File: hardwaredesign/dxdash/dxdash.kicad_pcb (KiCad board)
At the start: 2 copper layers, 112 parts, among them J11 spare, J12 spare, J13 spare, J14 spare, J15 spare, J16 uC_NRST, J17 3V3_uC, J18 SWO, J2 Conn_01x08_Pin, J3 CAN, J4 DEBUG, J5 UART, J6 12V_in, J8 Power Low Side Outputs, J9 Temps, Q2 NCV8402xST, Q3 NCV8402xST, U2 SN65HVD234, U3 STM32F103RETx, U4 TPS54302, U6 AMS1117-3.3, U7 74HCT04, Y2 8MHz

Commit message: controller board added features
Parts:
- removed C77, C78, C79: 100nF, Capacitor_SMD:C_1206_3216Metric_Pad1.33x1.80mm_HandSolder
- removed J11, J13, J14, J15: spare, Connector_PinHeader_2.54mm:PinHeader_1x06_P2.54mm_Vertical
- removed J3: CAN, Connector_PinHeader_2.54mm:PinHeader_1x03_P2.54mm_Vertical
- removed J9: Temps, Connector_PinHeader_2.54mm:PinHeader_1x04_P2.54mm_Vertical
- removed JP1: SolderJumper3V3together, Jumper:SolderJumper-2_P1.3mm_Open_TrianglePad1.0x1.5mm
- removed R31, R33, R35: 10k, Resistor_SMD:R_1206_3216Metric_Pad1.30x1.75mm_HandSolder
- removed R32, R34, R36: 47k, Resistor_SMD:R_1206_3216Metric_Pad1.30x1.75mm_HandSolder
- removed TP14, TP23, TP24, TP34, TP36: ~, TestPoint:TestPoint_THTPad_D1.0mm_Drill0.5mm
- added C1: 100n, Capacitor_SMD:C_1206_3216Metric_Pad1.33x1.80mm_HandSolder, F.Cu at (58.1, 77.4)
- added C2: 100nF, Capacitor_SMD:C_1206_3216Metric_Pad1.33x1.80mm_HandSolder, F.Cu at (44.7, 129.5)
- added C3: 100nF, Capacitor_SMD:C_1206_3216Metric_Pad1.33x1.80mm_HandSolder, F.Cu at (44.7, 132.9)
- added H4: MountingHole, MountingHole:MountingHole_3.5mm, F.Cu at (215.8, 133.8)
- added H5: MountingHole, MountingHole:MountingHole_3.5mm, F.Cu at (124.2, 81.2)
- added H6: MountingHole, MountingHole:MountingHole_3.5mm, F.Cu at (227.3, 81.0)
- added H7: MountingHole, MountingHole:MountingHole_3.5mm, F.Cu at (127.7, 147.0)
- added H8: MountingHole, MountingHole:MountingHole_3.5mm, F.Cu at (227.2, 145.1)
- added J1: Conn_01x08_Pin, Connector_PinHeader_2.54mm:PinHeader_1x08_P2.54mm_Vertical, F.Cu at (216.8, 102.5)
- added Q4: BC556, Package_TO_SOT_THT:TO-92_Inline, F.Cu at (40.1, 99.9)
- added Q6: BC546, Package_TO_SOT_THT:TO-92_Inline, F.Cu at (40.1, 105.7)
- added Q7: BC556, Package_TO_SOT_THT:TO-92_Inline, F.Cu at (50.5, 79.0)
- added Q8: BC546, Package_TO_SOT_THT:TO-92_Inline, F.Cu at (50.5, 84.8)
- added R1: 10k, Resistor_SMD:R_1206_3216Metric_Pad1.30x1.75mm_HandSolder, F.Cu at (40.0, 113.0)
- added R10: 4k7, Resistor_SMD:R_1206_3216Metric_Pad1.30x1.75mm_HandSolder, F.Cu at (45.6, 87.3)
- added R2: 1k, Resistor_SMD:R_1206_3216Metric_Pad1.30x1.75mm_HandSolder, F.Cu at (47.6, 98.3)
- added R25: 47k, Resistor_SMD:R_1206_3216Metric_Pad1.30x1.75mm_HandSolder, F.Cu at (45.9, 116.3)
- added R26: 47k, Resistor_SMD:R_1206_3216Metric_Pad1.30x1.75mm_HandSolder, F.Cu at (45.9, 119.6)
- added R27: 47k, Resistor_SMD:R_1206_3216Metric_Pad1.30x1.75mm_HandSolder, F.Cu at (45.9, 122.9)
- added R28: 47k, Resistor_SMD:R_1206_3216Metric_Pad1.30x1.75mm_HandSolder, F.Cu at (45.9, 126.2)
- added R3: 10k, Resistor_SMD:R_1206_3216Metric_Pad1.30x1.75mm_HandSolder, F.Cu at (40.0, 116.3)
- added R39: 47k, Resistor_SMD:R_1206_3216Metric_Pad1.30x1.75mm_HandSolder, F.Cu at (51.9, 113.0)
- added R4: 10k, Resistor_SMD:R_1206_3216Metric_Pad1.30x1.75mm_HandSolder, F.Cu at (47.6, 101.6)
- added R40: 47k, Resistor_SMD:R_1206_3216Metric_Pad1.30x1.75mm_HandSolder, F.Cu at (51.9, 116.3)
- added R41: 100, Resistor_SMD:R_1206_3216Metric_Pad1.30x1.75mm_HandSolder, F.Cu at (51.9, 119.6)
- added R5: 10k, Resistor_SMD:R_1206_3216Metric_Pad1.30x1.75mm_HandSolder, F.Cu at (40.0, 119.6)
- added R6: 10k, Resistor_SMD:R_1206_3216Metric_Pad1.30x1.75mm_HandSolder, F.Cu at (47.6, 104.9)
- added R7: 4k7, Resistor_SMD:R_1206_3216Metric_Pad1.30x1.75mm_HandSolder, F.Cu at (45.6, 77.4)
- added R8: 10k, Resistor_SMD:R_1206_3216Metric_Pad1.30x1.75mm_HandSolder, F.Cu at (45.6, 80.7)
- added R9: 4k7, Resistor_SMD:R_1206_3216Metric_Pad1.30x1.75mm_HandSolder, F.Cu at (45.6, 84.0)
- added SW1: SW_Push, Button_Switch_THT:SW_PUSH_6mm_H5mm, F.Cu at (136.8, 146.3)
- added SW2: SW_Push, Button_Switch_THT:SW_PUSH_6mm_H5mm, F.Cu at (215.1, 151.9)
- added SW3: SW_Push, Button_Switch_THT:SW_PUSH_6mm_H5mm, F.Cu at (198.4, 142.4)
- added SW4: SW_Push, Button_Switch_THT:SW_PUSH_6mm_H5mm, F.Cu at (177.6, 147.2)
- added SW5: SW_Push, Button_Switch_THT:SW_PUSH_6mm_H5mm, F.Cu at (154.7, 141.9)
- added TP2: ~, TestPoint:TestPoint_THTPad_D1.0mm_Drill0.5mm, F.Cu at (58.4, 112.9)
- added TP3: ~, TestPoint:TestPoint_THTPad_D1.0mm_Drill0.5mm, F.Cu at (58.4, 116.0)
- D11: value STATEC -> LED2
- D12: value CONTACTOR1 -> LED3
- H1, H2, H3: footprint MountingHole:MountingHole_3.2mm_M3 -> MountingHole:MountingHole_3.5mm
- J12: value spare -> CAN; footprint Connector_PinHeader_2.54mm:PinHeader_1x06_P2.54mm_Vertical -> Connector_PinHeader_2.54mm:PinHeader_1x03_P2.54mm_Vertical
- J2: value Conn_01x08_Pin -> Conn_01x06_Pin; footprint Connector_PinHeader_2.54mm:PinHeader_1x08_P2.54mm_Vertical -> Connector_PinHeader_2.54mm:PinHeader_1x06_P2.54mm_Vertical
- R11, R12, R13: value 220 -> 10k
- R14: value 220 -> 47k
- R16: value 1k -> 47k
- moved R16 129.6 mm to (45.9, 113.0), turned to 0 degrees
- moved R14 127.9 mm to (40.0, 126.2)
- moved R13 121.7 mm to (40.0, 122.9)
- moved R11 105.4 mm to (45.6, 90.6)
- moved H2 103.0 mm to (215.8, 88.8)
- moved R12 99.9 mm to (45.6, 93.9)
- moved J12 91.3 mm to (52.9, 99.0)
- moved H3 63.1 mm to (139.8, 133.8)
- moved TP1 49.8 mm to (110.1, 96.7)
- moved H1 47.5 mm to (139.8, 88.8)
- moved U2 46.0 mm to (176.8, 100.7)
- moved C58 45.3 mm to (152.3, 115.3)
- moved C60 45.3 mm to (138.7, 103.4)
- moved C61 45.3 mm to (149.3, 116.2)
- moved R19 45.3 mm to (142.9, 130.1)
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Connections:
- C65 pad 2: 24V_P -> 24V_SWITCHED
- J12 pad 1: unconnected-(J12-Pin_1-Pad1) -> CANL
- J12 pad 2: unconnected-(J12-Pin_2-Pad2) -> GND
- J12 pad 3: unconnected-(J12-Pin_3-Pad3) -> CANH
- J2 pad 1: GND -> Net-(J2-Pin_1)
- J2 pad 2: 3V3_D -> Net-(J2-Pin_1)
- J2 pad 3: RESET# -> Net-(J2-Pin_3)
- J2 pad 4: SERIAL_IO_4_MOSI -> Net-(J2-Pin_4)
- J2 pad 5: SERIAL_IO_3_MISO -> GND
- J2 pad 6: SERIAL_IO_2_CS -> GND
- R11 pad 1: SPI1_NSS -> uC_pwr_button
- R11 pad 2: SERIAL_IO_2_CS -> Net-(R10-Pad2)
- R12 pad 1: SPI1_CLK -> uC_pwr_button
- R12 pad 2: SERIAL_IO_1_CLK -> GND
- R13 pad 1: SPI1_MISO -> 3V3_uC
- R13 pad 2: SERIAL_IO_3_MISO -> Net-(R13-Pad2)
- R14 pad 1: SPI1_MOSI -> Net-(R13-Pad2)
- R14 pad 2: SERIAL_IO_4_MOSI -> uC_button4
- R16 pad 1: CANL -> Net-(R16-Pad1)
- R16 pad 2: CANH -> uC_button3
- U2 pad 5: 3V3_uC -> Net-(JP5-C)
- U3 pad 10: ADC123_IN12 -> Net-(U3-PC2)
- U3 pad 11: ADC_U_HVDC -> Net-(U3-PC3)
- U3 pad 26: Net-(U3-PB0) -> DISPLAY_DC
- U3 pad 27: Net-(U3-PB1) -> DISPLAY_RES
- U3 pad 33: Net-(U3-PB12) -> BUSWAKE
- U3 pad 34: Net-(U3-PB13) -> KEEP_ON
- U3 pad 43: Net-(U3-PA10) -> uC_pwr_button
- U3 pad 8: ADC123_IN10 -> uC_pot1
- U3 pad 9: ADC123_IN11 -> uC_pot2
- U4 pad 3: 24V_P -> 24V_SWITCHED
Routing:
- net RESET#: track 33.3 -> 0.00 mm, vias 1 -> 0
- net ADC_U_HVDC: track 23.4 -> 0.00 mm
- net Net-(U3-PC3): track 0.00 -> 23.4 mm
- net SPI1_MOSI: track 36.4 -> 14.1 mm
- net SPI1_MISO: track 31.4 -> 14.2 mm
- net Net-(U3-PC2): track 0.00 -> 16.2 mm
- net ADC123_IN12: track 16.2 -> 0.00 mm
- net SPI1_NSS: track 30.5 -> 14.7 mm
- net Net-(J9-Pin_3): track 14.4 -> 0.00 mm
- net Net-(J9-Pin_2): track 12.7 -> 0.00 mm
- net ADC123_IN10: track 12.6 -> 0.00 mm
- net ADC123_IN11: track 12.3 -> 0.00 mm
- net CANL: track 11.4 -> 0.00 mm
- net Net-(U3-PB1): track 10.8 -> 0.00 mm
- net DISPLAY_RES: track 0.00 -> 10.8 mm
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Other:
- board text added: "DXBUS controller github.com/uhi22/invacare-g50-investigations version 2024-11-12"
- board text removed: "3V3"
- board text removed: "CLK"
- board text removed: "CP"
- board text removed: "CS"
- board text removed: "GND"
- board text removed: "INT"
- board text removed: "MISO"
- board text removed: "MOSI"
- board text removed: "RES"
- board text removed: "fully open CCS charge controller github.com/uhi22/foccci version 2023-07-12"

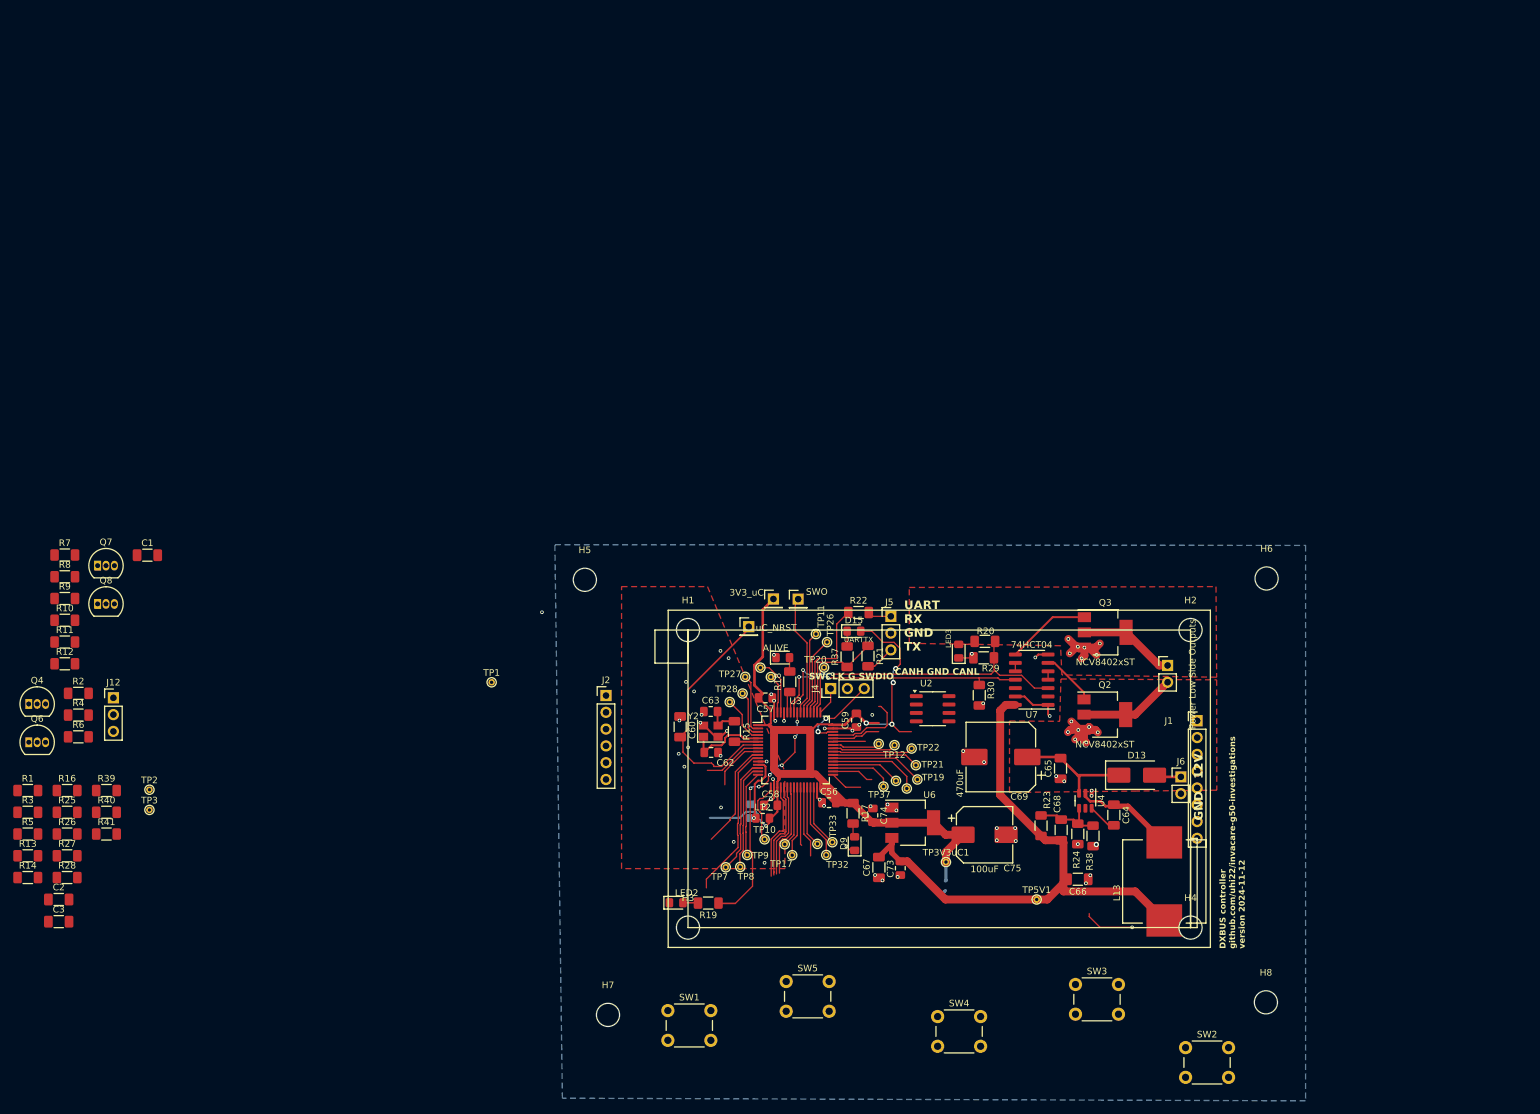
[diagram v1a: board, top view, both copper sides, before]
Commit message: added joystick
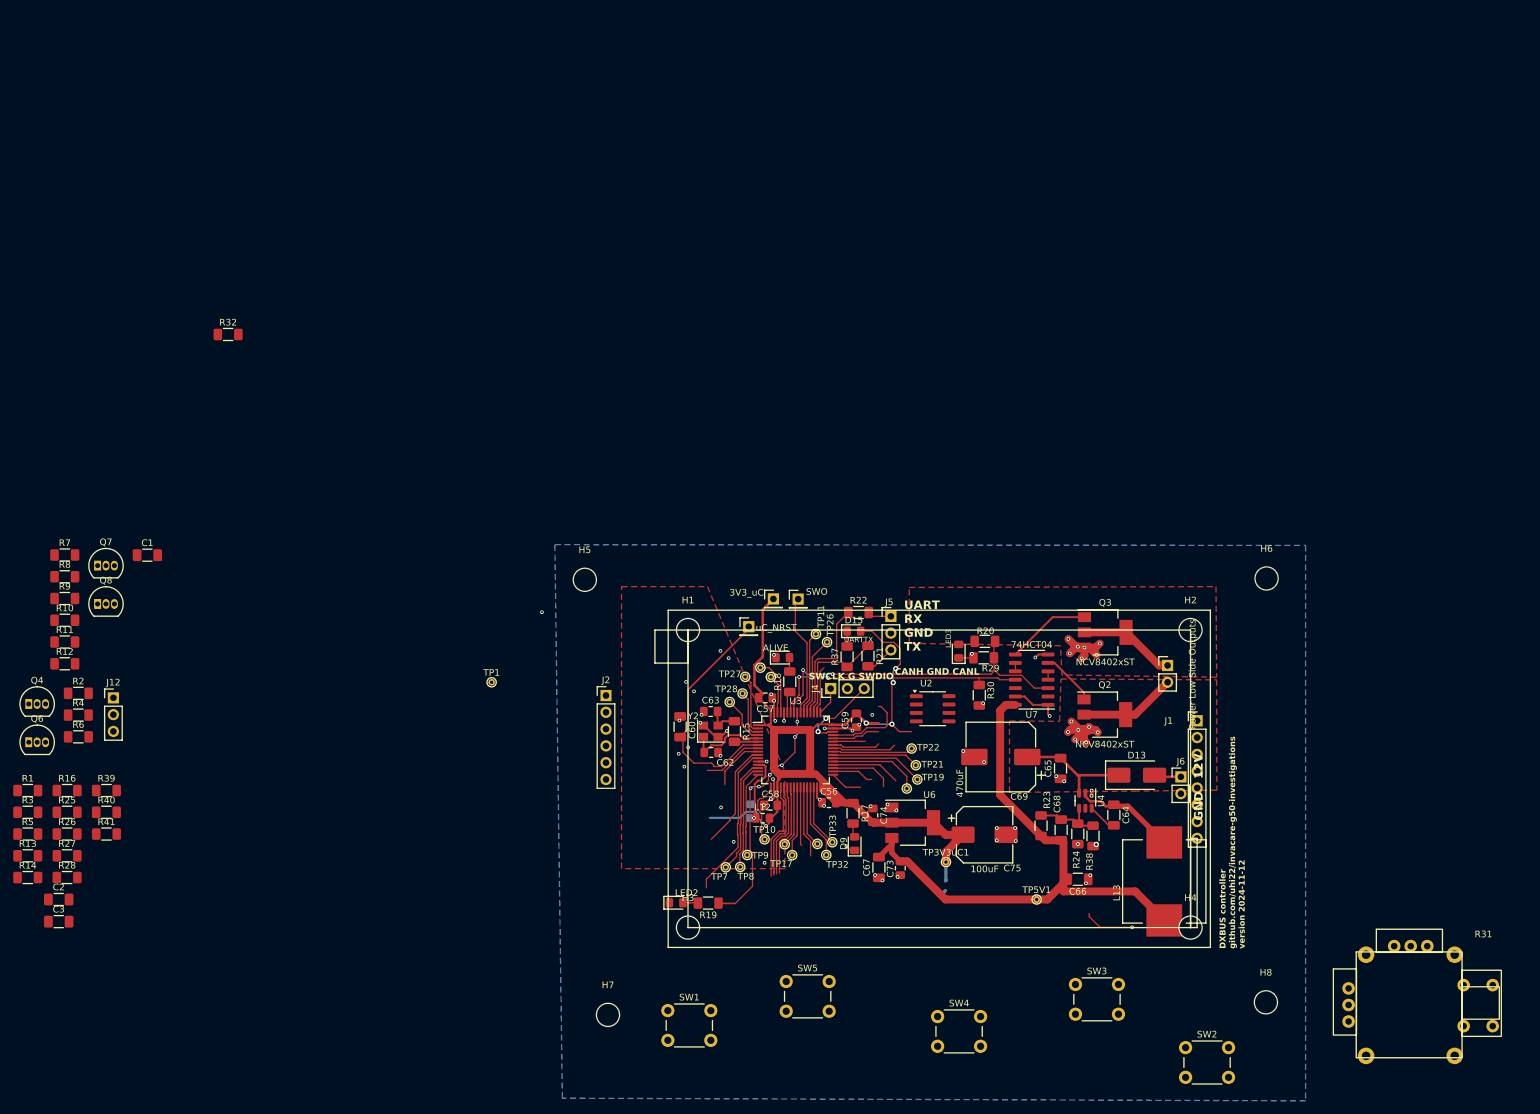
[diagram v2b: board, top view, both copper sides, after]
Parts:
- removed TP12, TP13, TP2, TP20, TP3, TP37, TP38: ~, TestPoint:TestPoint_THTPad_D1.0mm_Drill0.5mm
- added R31: Joystick, libJoystick:joystickXYButton, F.Cu at (249.1, 145.5)
- added R32: 10k, Resistor_SMD:R_1206_3216Metric_Pad1.30x1.75mm_HandSolder, F.Cu at (70.3, 44.1)
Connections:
- U3 pad 10: Net-(U3-PC2) -> uC_joystickX
- U3 pad 11: Net-(U3-PC3) -> uC_joystickY
- U3 pad 35: Net-(U3-PB14) -> uC_button2
- U3 pad 36: Net-(U3-PB15) -> uC_button3
- U3 pad 41: Net-(U3-PA8) -> uC_button1
- U3 pad 42: Net-(U3-PA9) -> uC_joystickbutton
- U3 pad 50: Net-(U3-PA15) -> unconnected-(U3-PA15-Pad50)
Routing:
- net uC_joystickY: track 0.00 -> 23.4 mm
- net Net-(U3-PC3): track 23.4 -> 0.00 mm
- net uC_joystickX: track 0.00 -> 16.2 mm
- net Net-(U3-PC2): track 16.2 -> 0.00 mm
- net uC_button3: track 0.00 -> 10.5 mm
- net Net-(U3-PB15): track 10.5 -> 0.00 mm
- net uC_button1: track 0.00 -> 9.67 mm
- net Net-(U3-PA8): track 9.67 -> 0.00 mm
- net uC_button2: track 0.00 -> 9.50 mm
- net Net-(U3-PB14): track 9.50 -> 0.00 mm
- net uC_joystickbutton: track 0.00 -> 7.24 mm
- net Net-(U3-PA9): track 7.24 -> 0.00 mm
- net unconnected-(U3-PA15-Pad50): track 0.00 -> 7.22 mm
- net Net-(U3-PA15): track 7.22 -> 0.00 mm

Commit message: added screw terminals
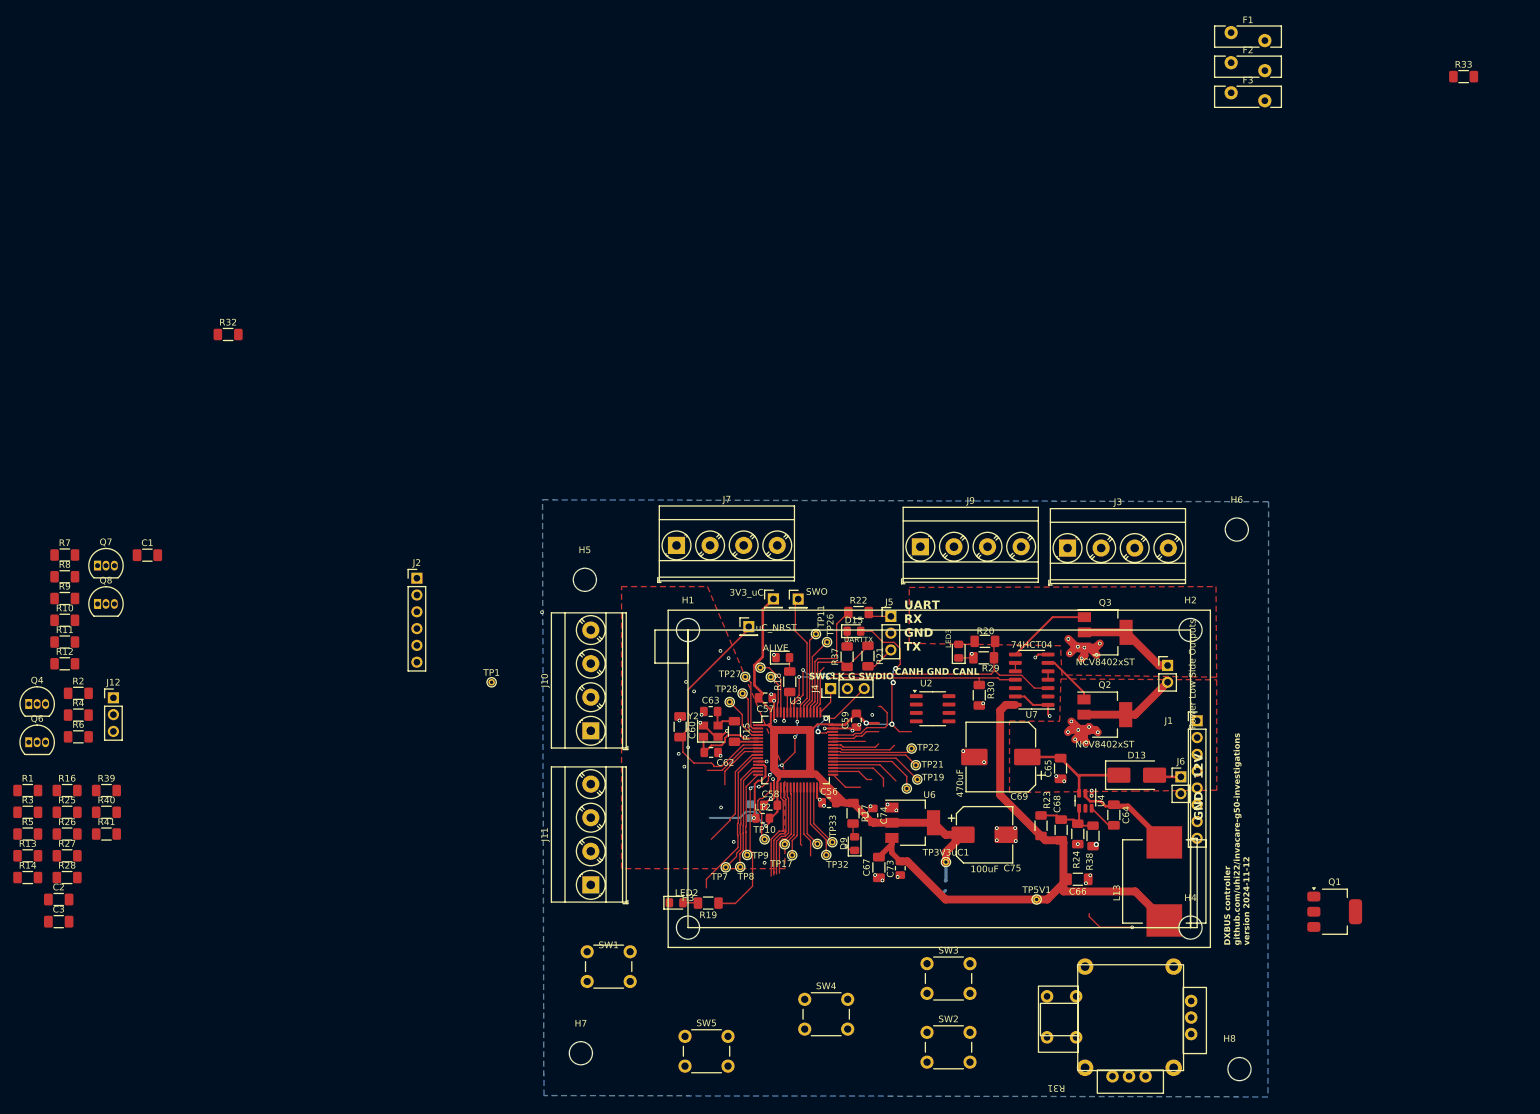
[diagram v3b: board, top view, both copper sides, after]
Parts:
- added F1: Polyfuse, Fuse:Fuse_Bourns_MF-RG400, F.Cu at (222.0, -1.59)
- added F2: Polyfuse, Fuse:Fuse_Bourns_MF-RG400, F.Cu at (222.0, 2.96)
- added F3: Polyfuse, Fuse:Fuse_Bourns_MF-RG400, F.Cu at (222.0, 7.51)
- added J10: Screw_Terminal_01x04, TerminalBlock_Phoenix:TerminalBlock_Phoenix_MKDS-3-4-5.08_1x04_P5.08mm_Horizontal, F.Cu at (125.1, 104.0)
- added J11: Screw_Terminal_01x04, TerminalBlock_Phoenix:TerminalBlock_Phoenix_MKDS-3-4-5.08_1x04_P5.08mm_Horizontal, F.Cu at (125.1, 127.3)
- added J3: Screw_Terminal_01x04, TerminalBlock_Phoenix:TerminalBlock_Phoenix_MKDS-3-4-5.08_1x04_P5.08mm_Horizontal, F.Cu at (197.2, 76.4)
- added J7: Screw_Terminal_01x04, TerminalBlock_Phoenix:TerminalBlock_Phoenix_MKDS-3-4-5.08_1x04_P5.08mm_Horizontal, F.Cu at (138.1, 76.0)
- added J9: Screw_Terminal_01x04, TerminalBlock_Phoenix:TerminalBlock_Phoenix_MKDS-3-4-5.08_1x04_P5.08mm_Horizontal, F.Cu at (175.0, 76.2)
- added Q1: NCV8402xST, Package_TO_SOT_SMD:SOT-223, F.Cu at (237.6, 131.4)
- added R33: 10k, Resistor_SMD:R_1206_3216Metric_Pad1.30x1.75mm_HandSolder, F.Cu at (257.1, 5.06)
- moved R31 42.6 mm to (206.5, 147.4), turned to 180 degrees
- moved SW2 39.2 mm to (176.0, 149.6)
- moved J2 33.7 mm to (98.8, 80.9)
- moved SW3 22.7 mm to (176.0, 139.2)
- moved SW4 20.3 mm to (157.5, 144.6)
- moved SW5 17.4 mm to (139.4, 150.2)
- moved SW1 15.1 mm to (124.6, 137.4)
- moved H8 10.9 mm to (223.2, 155.2)
- moved H6 8.66 mm to (222.8, 73.6)
- moved H7 7.10 mm to (123.6, 152.8)
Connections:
- net Net-(J2-Pin_1) renamed pot5V
- net Net-(J2-Pin_3) renamed pot1
- net Net-(J2-Pin_4) renamed pot2
- net Net-(R1-Pad2) renamed button1
- net Net-(R13-Pad2) renamed button4
- net Net-(R16-Pad1) renamed button3
- net Net-(R25-Pad1) renamed button2
- Q2 pad 2: OUT1_LS -> Net-(F1-Pad1)
- Q2 pad 4: OUT1_LS -> Net-(F1-Pad1)
- Q3 pad 2: OUT2_LS -> Net-(F2-Pad1)
- Q3 pad 4: OUT2_LS -> Net-(F2-Pad1)
- U7 pad 1: GND -> OUT_CONTROL3
- U7 pad 12: unconnected-(U7-Pad12) -> Net-(Q1-G)
- U7 pad 13: GND -> Net-(U7-Pad13)
- U7 pad 2: unconnected-(U7-Pad2) -> Net-(U7-Pad13)
